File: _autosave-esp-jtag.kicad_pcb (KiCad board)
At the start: 2 copper layers, 57.2 x 35.6 mm, 70 parts, among them J1 USB_B_Micro, J2 JTAG, Q1 WST03P06, Q2 S8050, Q3 S8050, SW1 SW_SPST, SW2 SW_SPST, U1 74AHC1GU04, U2 SN74AHC125RGY, U3 AMS1117-3.3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

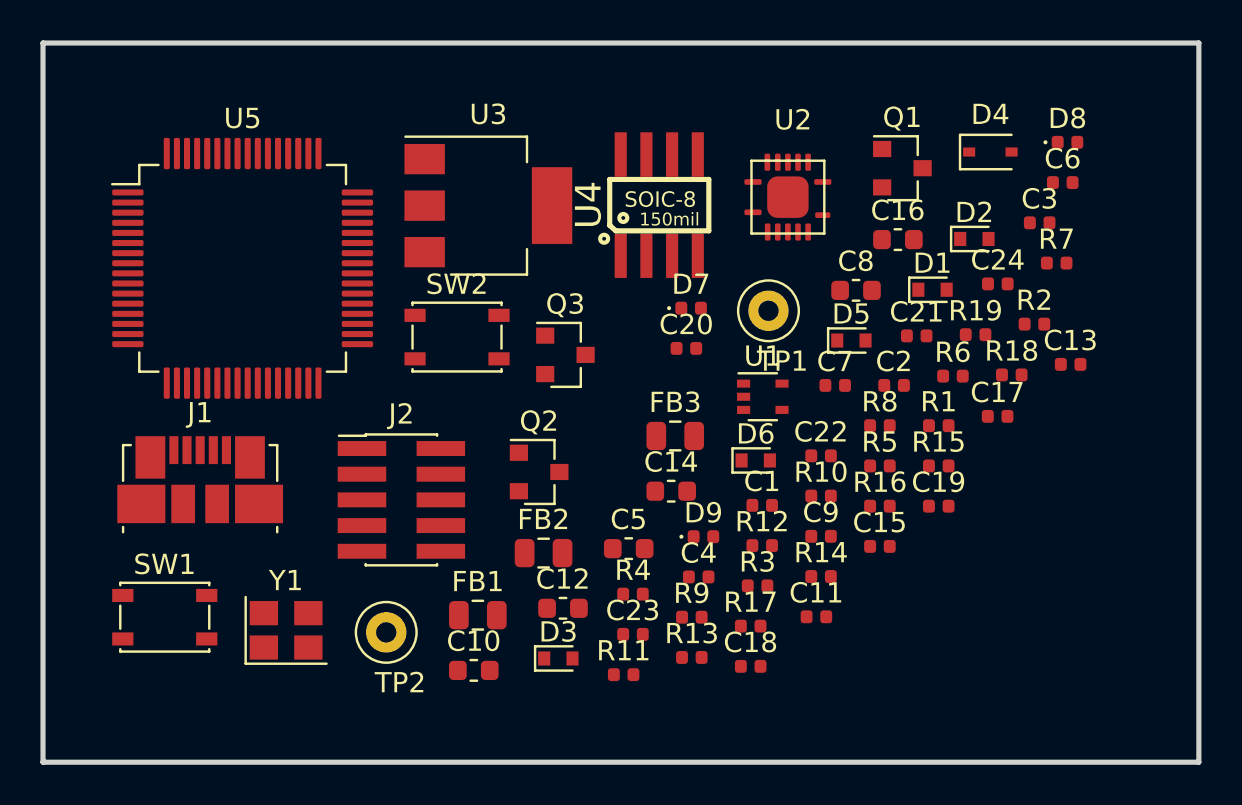
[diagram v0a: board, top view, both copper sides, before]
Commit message: Layout and route the PCB
Prepare the PCB layout by arranging the components
Route all traces and rectify mistakes in the connections
Add ground pours on top and bottom copper
Update the preview images and the README file
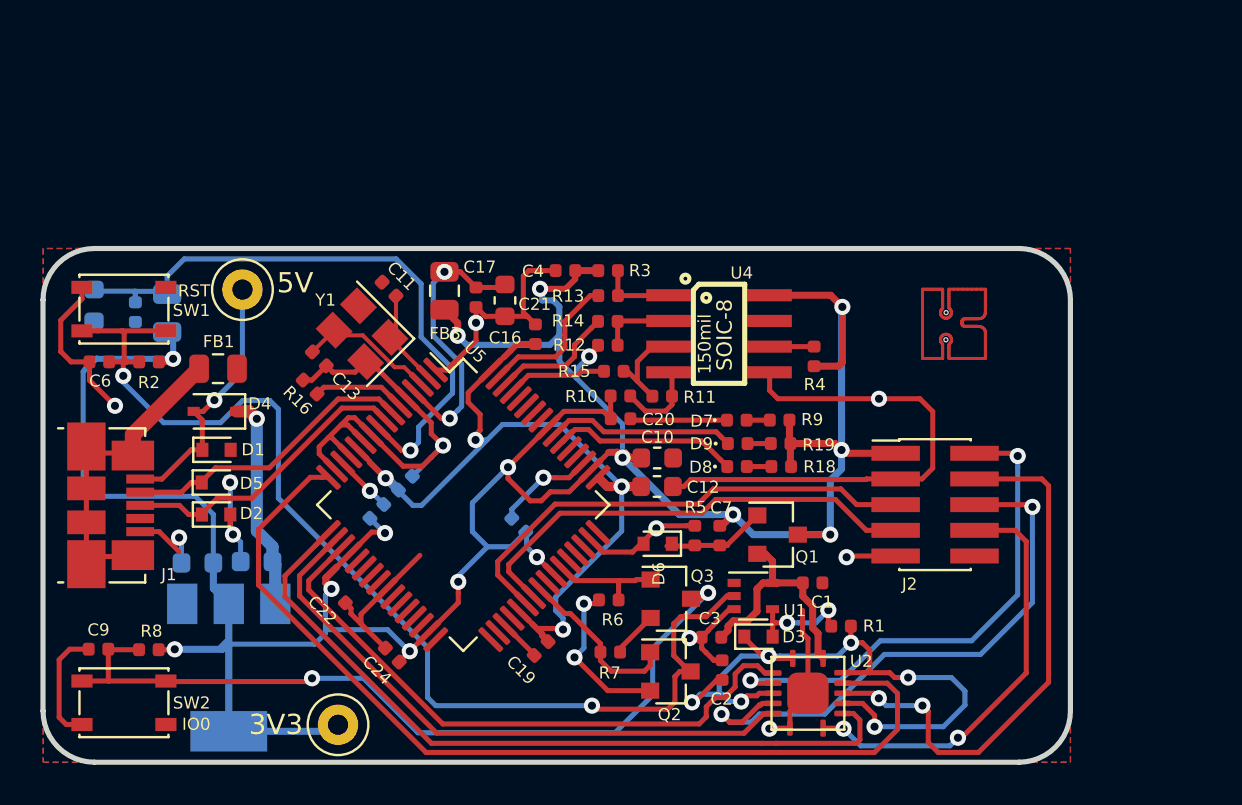
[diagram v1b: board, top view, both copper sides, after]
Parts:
- added L1: karibe_logo, artwork:karibe_logo, F.Cu at (235.2, 133.3)
- C14, C15, C18, C23, C5, C8, FB2, R17, U3: moved to B.Cu
- moved C6 48.5 mm to (193.3, 135.1), turned to 180 degrees
- moved R2 43.8 mm to (195.7, 135.1), turned to 180 degrees
- moved D4 40.4 mm to (199.0, 137.6), turned to 180 degrees
- moved D2 39.9 mm to (199.1, 142.7)
- moved C15 38.6 mm to (195.1, 132.7), turned to 270 degrees
- moved R8 37.8 mm to (195.7, 149.4), turned to 180 degrees
- moved C13 37.1 mm to (204.2, 135.0), turned to 315 degrees
- moved D1 36.3 mm to (199.1, 139.5)
- moved C9 36.2 mm to (193.2, 149.4), turned to 180 degrees
- moved C8 35.2 mm to (198.1, 145.1), turned to 180 degrees
- moved C24 35.1 mm to (207.8, 149.6), turned to 135 degrees
- moved D5 32.2 mm to (199.0, 141.1)
- moved C14 30.0 mm to (193.0, 132.4), turned to 270 degrees
- moved R7 29.3 mm to (218.5, 149.5)
- moved R16 28.8 mm to (203.7, 136.4), turned to 135 degrees
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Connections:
- J2 pad 10: (no net) -> GND
- J2 pad 2: FT_TMS -> ESP_TMS
- J2 pad 4: FT_TCK -> ESP_TCK
- J2 pad 5: FT_RxD -> FT_TxD
- J2 pad 6: FT_TDO -> ESP_TDO
- J2 pad 7: FT_TxD -> FT_RxD
- J2 pad 8: FT_TDI -> ESP_TDI
- U2 pad 11: (no net) -> ESP_TCK
- U2 pad 3: (no net) -> ESP_TMS
- U2 pad 5: (no net) -> ESP_TDO
- U2 pad 8: (no net) -> ESP_TDI
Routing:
- net VDD3V3: track 0.00 -> 165.7 mm, vias 0 -> 16
- net GND: track 0.00 -> 123.2 mm, vias 0 -> 12
- net ESP_EN: track 0.00 -> 55.9 mm, vias 0 -> 2
- net FT_TCK: track 0.00 -> 47.5 mm
- net VDD1V8: track 0.00 -> 41.6 mm, vias 0 -> 4
- net ESP_IO0_B: track 0.00 -> 40.4 mm, vias 0 -> 2
- net FT_TDI: track 0.00 -> 37.5 mm
- net ESP_EN_N: track 0.00 -> 34.8 mm, vias 0 -> 6
- net Net-(C14-Pad1): track 0.00 -> 30.9 mm, vias 0 -> 1
- net FT_TMS: track 0.00 -> 30.5 mm
- net FT_TDO: track 0.00 -> 30.2 mm
- net ESP_TDO: track 0.00 -> 28.7 mm, vias 0 -> 2
- net ESP_TCK: track 0.00 -> 27.2 mm, vias 0 -> 2
- net ESP_TMS: track 0.00 -> 25.2 mm, vias 0 -> 2
- net FT_TxD: track 0.00 -> 24.2 mm
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- added copper zone on B.Cu, net GND
- added copper zone on F.Cu, net GND
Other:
- board size 57.2 x 35.6 mm -> 50.8 x 25.4 mm
- net class 1V8 added: clearance 0.2, trace_width 0.3, via_dia 0.8, via_drill 0.4
- net class 3V3 added: clearance 0.2, trace_width 0.3, via_dia 0.8, via_drill 0.4
- net class 5V added: clearance 0.25, trace_width 0.6, via_dia 1, via_drill 0.6
- net class crystal added: clearance 0.1, trace_width 0.2, via_dia 0.8, via_drill 0.4
- board text added: "3V3"
- board text added: "5V"
- board text added: "IO0"
- board text added: "RST"
